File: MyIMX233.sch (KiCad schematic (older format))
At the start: 40 parts, among them IC1 iMX233, IC2 DDR_SDRAM_MT46_x16, J1 USB_A, J2 Micro_SD_Card, SW1 SWITCH_PUSHBUTTON, Y1 24Mhz

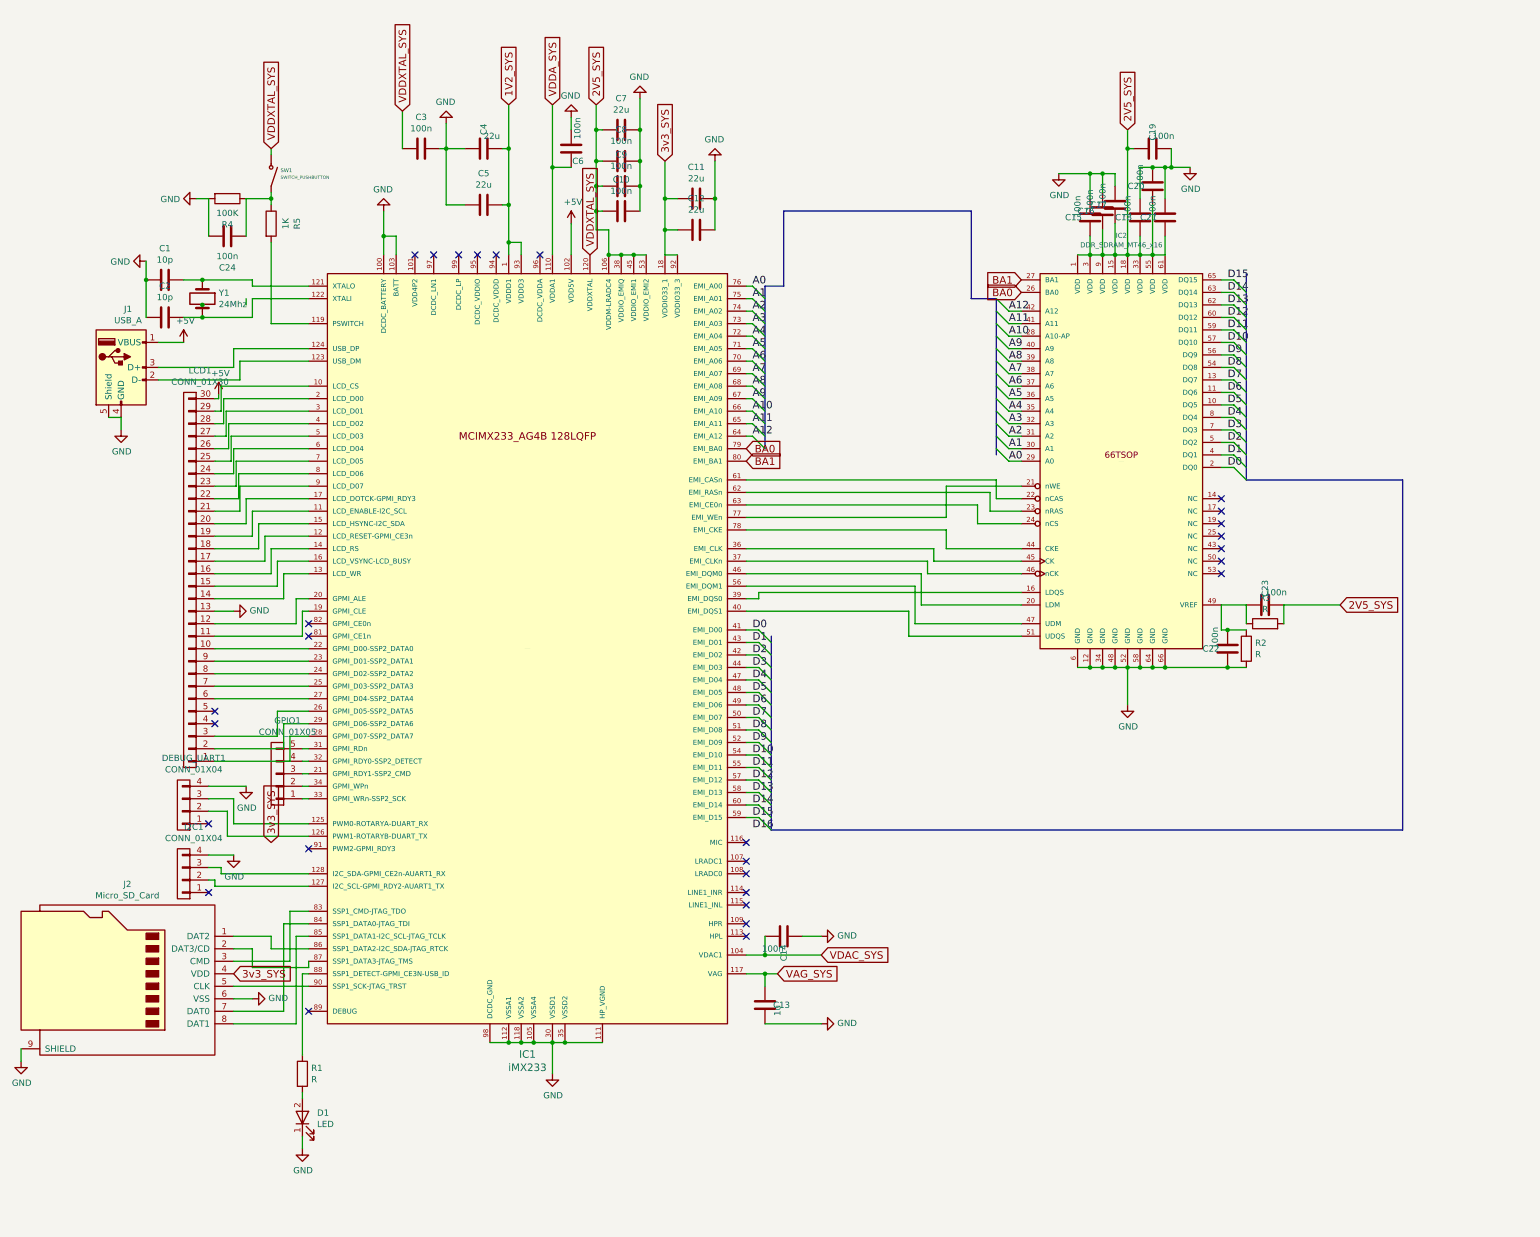
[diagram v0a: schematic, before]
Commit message: footprint mapped
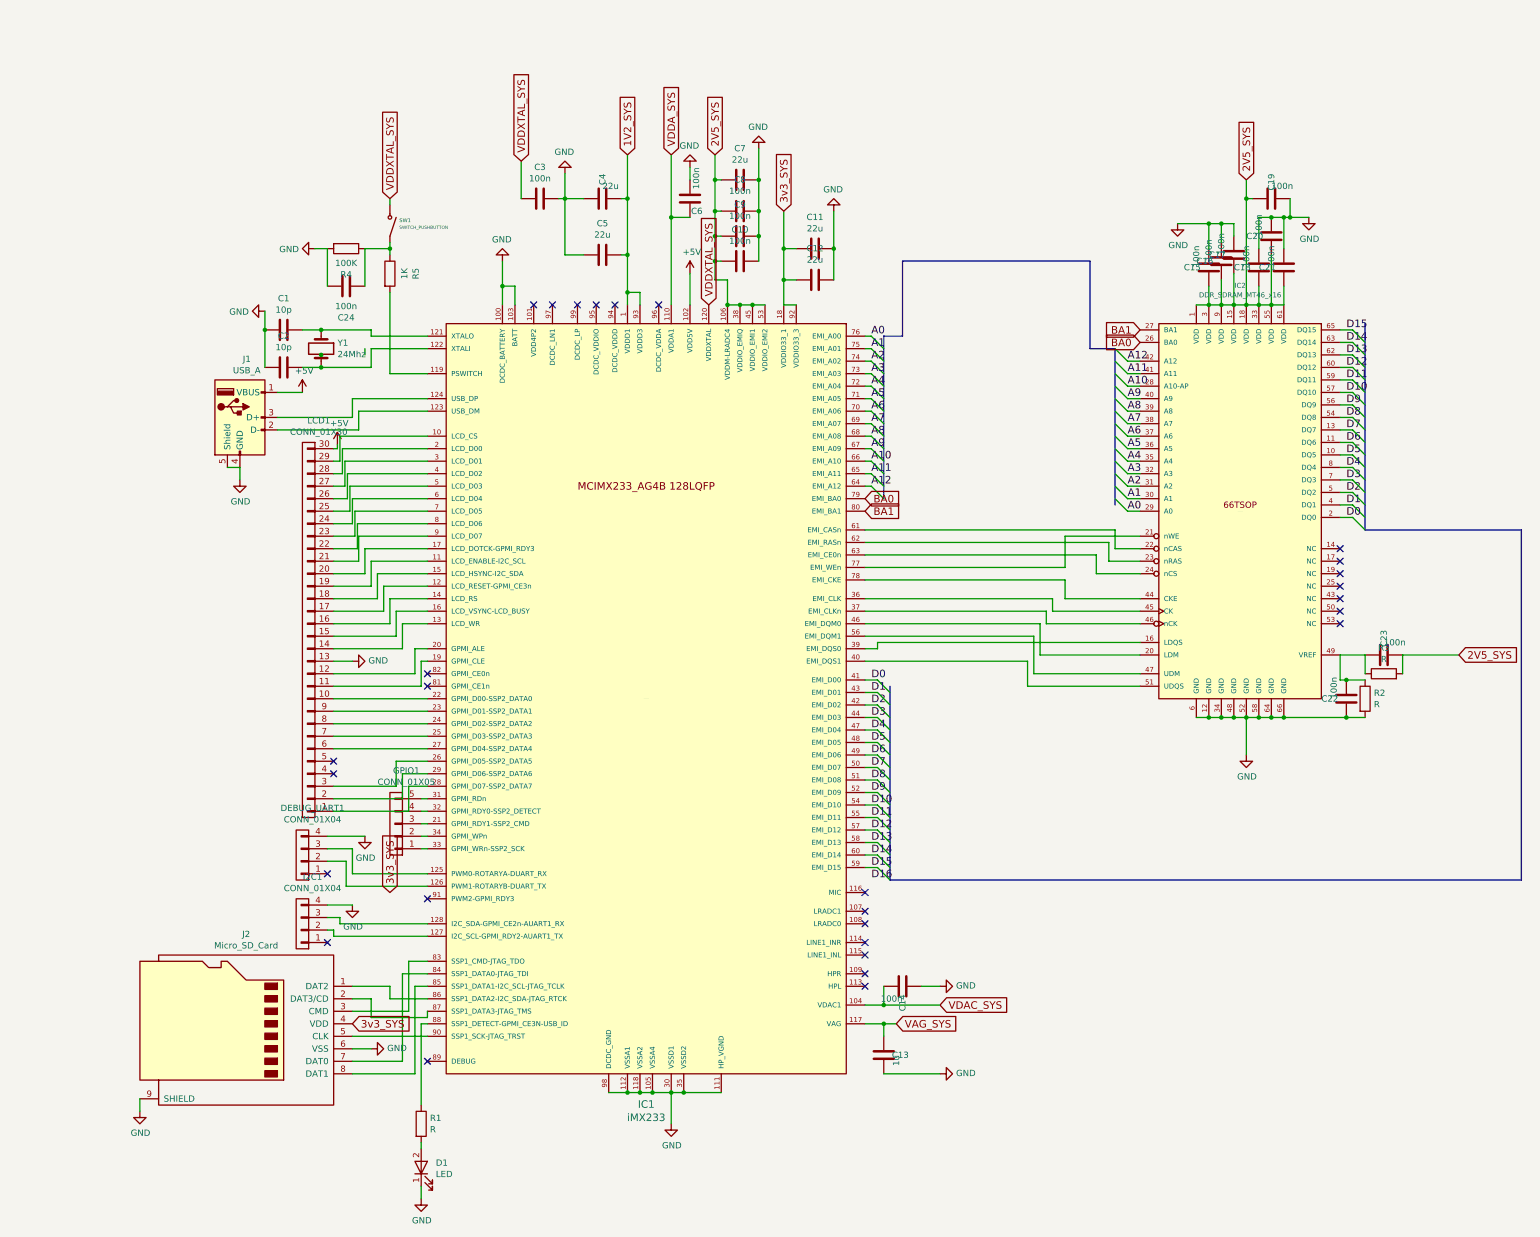
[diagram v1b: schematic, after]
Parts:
- C1, C10, C11, C12, C13, C14, C15, C16, C17, C18, C19, C2, C20, C21, C22, C23, C24, C3, C4, C5, C6, C7, C8, C9: footprint (none) -> Capacitors_SMD:C_0805_HandSoldering
- D1: footprint (none) -> LEDs:LED_D4.0mm
- DEBUG_UART1, I2C1: footprint (none) -> Pin_Headers:Pin_Header_Straight_1x04_Pitch2.54mm
- GPIO1: footprint (none) -> Pin_Headers:Pin_Header_Straight_1x05_Pitch2.54mm
- IC1: footprint (none) -> Housings_QFP:LQFP-128_14x14mm_Pitch0.4mm
- IC2: footprint (none) -> opendous:TSOP66_JEDEC_DDR_SDRAM
- J1: footprint (none) -> Connectors:USB_Micro-B
- J2: footprint (none) -> Connectors_Hirose:microSD_Card_Receptacle_Hirose_DM3AT-SF-PEJM5
- LCD1: footprint (none) -> Pin_Headers:Pin_Header_Straight_1x30_Pitch2.54mm
- R1, R2, R3, R4, R5: footprint (none) -> Resistors_SMD:R_0805_HandSoldering
- SW1: footprint (none) -> Buttons_Switches_THT:SW_PUSH_6mm
- Y1: footprint (none) -> Crystals:Crystal_HC49-4H_Vertical
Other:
- moved on the sheet: C1, C10, C11, C12, C13, C14, C15, C16, C17, C18, C19, C2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

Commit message: pcb without length matching and plot
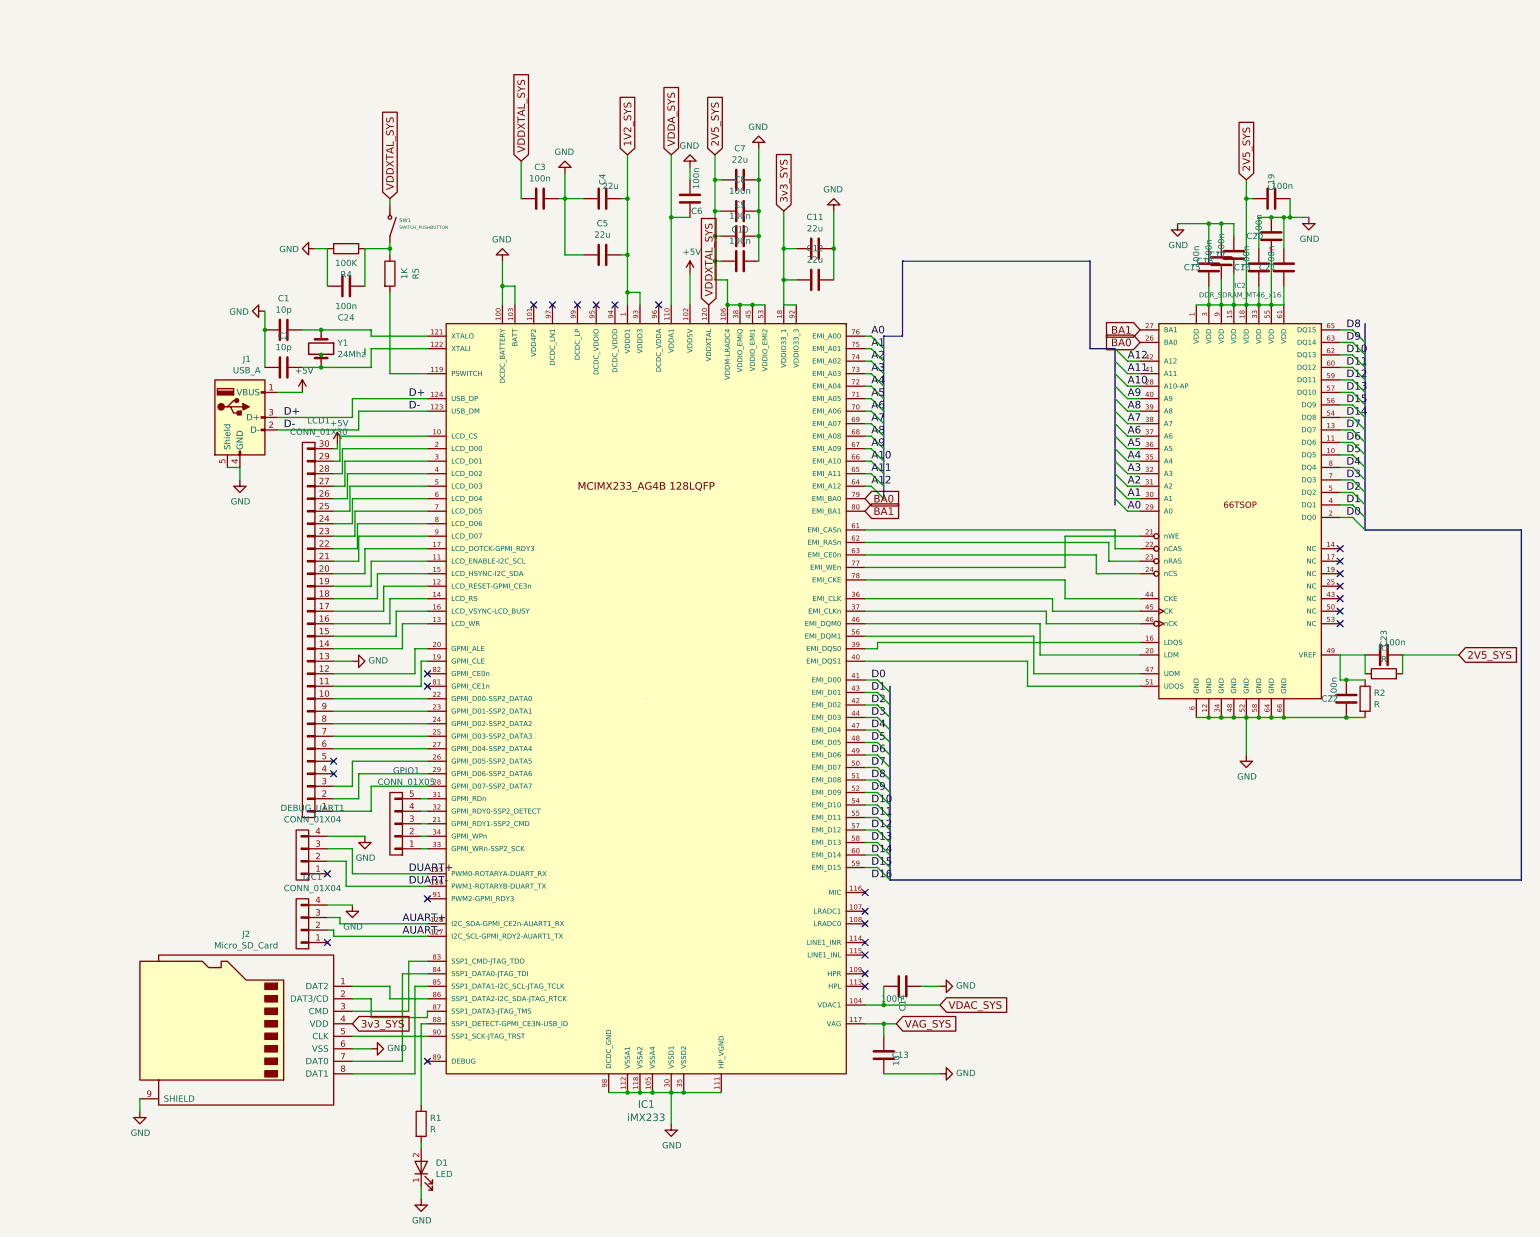
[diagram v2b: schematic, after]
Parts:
- C1, C10, C14, C15, C16, C17, C18, C19, C2, C20, C21, C22, C23, C24, C3, C6, C8, C9: footprint Capacitors_SMD:C_0805_HandSoldering -> Capacitors_SMD:C_0402
- C13: footprint Capacitors_SMD:C_0805_HandSoldering -> Capacitors_SMD:C_0603
- R1, R2, R3, R4, R5: footprint Resistors_SMD:R_0805_HandSoldering -> Resistors_SMD:R_0603
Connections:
- net D10: now also IC2.62 (DQ13); no longer IC2.57 (DQ10)
- net D11: now also IC2.60 (DQ12); no longer IC2.59 (DQ11)
- net D12: now also IC2.59 (DQ11); no longer IC2.60 (DQ12)
- net D13: now also IC2.57 (DQ10); no longer IC2.62 (DQ13)
- net D14: now also IC2.54 (DQ8); no longer IC2.63 (DQ14)
- net D15: now also IC2.56 (DQ9); no longer IC2.65 (DQ15)
- net D8: now also IC2.65 (DQ15); no longer IC2.54 (DQ8)
- net D9: now also IC2.63 (DQ14); no longer IC2.56 (DQ9)
- net D-: now reaches IC1.123 (USB_DM), J1.2 (D-)
- net D+: now reaches IC1.124 (USB_DP), J1.3 (D+)
- net DUART+: now reaches DEBUG_UART1.3 (P3), IC1.125 (PWM0-ROTARYA-DUART_RX)
- net DUART-: now reaches DEBUG_UART1.2 (P2), IC1.126 (PWM1-ROTARYB-DUART_TX)
- net AUART-: now reaches I2C1.2 (P2), IC1.127 (I2C_SCL-GPMI_RDY2-AUART1_TX)
- net AUART+: now reaches I2C1.3 (P3), IC1.128 (I2C_SDA-GPMI_CE2n-AUART1_RX)
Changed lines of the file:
@@
 F 0 "C8" V 5498 2000 50  0000 C CNN
 F 1 "100n" V 5589 2000 50  0000 C CNN
-F 2 "Capacitors_SMD:C_0805_HandSoldering" H 5788 1850 50  0001 C CNN
+F 2 "Capacitors_SMD:C_0402" H 5788 1850 50  0001 C CNN
 F 3 "" H 5750 2000 50  0001 C CNN
 	1    5750 2000
@@
 F 0 "C9" V 5498 2200 50  0000 C CNN
 F 1 "100n" V 5589 2200 50  0000 C CNN
-F 2 "Capacitors_SMD:C_0805_HandSoldering" H 5788 2050 50  0001 C CNN
+F 2 "Capacitors_SMD:C_0402" H 5788 2050 50  0001 C CNN
 F 3 "" H 5750 2200 50  0001 C CNN
 	1    5750 2200
@@
 F 0 "C10" V 5498 2400 50  0000 C CNN
 F 1 "100n" V 5589 2400 50  0000 C CNN
-F 2 "Capacitors_SMD:C_0805_HandSoldering" H 5788 2250 50  0001 C CNN
+F 2 "Capacitors_SMD:C_0402" H 5788 2250 50  0001 C CNN
 F 3 "" H 5750 2400 50  0001 C CNN
 	1    5750 2400
@@
 F 0 "C6" H 5450 1800 50  0000 R CNN
 F 1 "100n" V 5400 2150 50  0000 R CNN
-F 2 "Capacitors_SMD:C_0805_HandSoldering" H 5388 1750 50  0001 C CNN
+F 2 "Capacitors_SMD:C_0402" H 5388 1750 50  0001 C CNN
 F 3 "" H 5350 1900 50  0001 C CNN
 	1    5350 1900
@@
 F 0 "C3" V 4402 1900 50  0000 C CNN
 F 1 "100n" V 4311 1900 50  0000 C CNN
-F 2 "Capacitors_SMD:C_0805_HandSoldering" H 4188 1750 50  0001 C CNN
+F 2 "Capacitors_SMD:C_0402" H 4188 1750 50  0001 C CNN
 F 3 "" H 4150 1900 50  0001 C CNN
 	1    4150 1900
@@
 F 0 "C13" H 7100 8750 50  0000 R CNN
 F 1 "1u" V 7000 8750 50  0000 R CNN
-F 2 "Capacitors_SMD:C_0805_HandSoldering" H 6938 8600 50  0001 C CNN
+F 2 "Capacitors_SMD:C_0603" H 6938 8600 50  0001 C CNN
 F 3 "" H 6900 8750 50  0001 C CNN
 	1    6900 8750
@@
 F 0 "C14" H 7250 8200 50  0000 R CNN
 F 1 "100n" V 7150 8200 50  0000 R CNN
-F 2 "Capacitors_SMD:C_0805_HandSoldering" H 7088 8050 50  0001 C CNN
+F 2 "Capacitors_SMD:C_0402" H 7088 8050 50  0001 C CNN
 F 3 "" H 7050 8200 50  0001 C CNN
 	1    7050 8200
@@
 F 0 "C1" V 2352 2950 50  0000 C CNN
 F 1 "10p" V 2261 2950 50  0000 C CNN
-F 2 "Capacitors_SMD:C_0805_HandSoldering" H 2138 2800 50  0001 C CNN
+F 2 "Capacitors_SMD:C_0402" H 2138 2800 50  0001 C CNN
 F 3 "" H 2100 2950 50  0001 C CNN
 	1    2100 2950
@@
 F 0 "C2" V 2352 3250 50  0000 C CNN
 F 1 "10p" V 2261 3250 50  0000 C CNN
-F 2 "Capacitors_SMD:C_0805_HandSoldering" H 2138 3100 50  0001 C CNN
+F 2 "Capacitors_SMD:C_0402" H 2138 3100 50  0001 C CNN
 F 3 "" H 2100 3250 50  0001 C CNN
 	1    2100 3250
@@
 F 0 "C22" H 10800 5900 50  0000 R CNN
 F 1 "100n" V 10700 5900 50  0000 R CNN
-F 2 "Capacitors_SMD:C_0805_HandSoldering" H 10638 5750 50  0001 C CNN
+F 2 "Capacitors_SMD:C_0402" H 10638 5750 50  0001 C CNN
 F 3 "" H 10600 5900 50  0001 C CNN
 	1    10600 5900
@@
 F 0 "C23" H 11100 5550 50  0000 R CNN
 F 1 "100n" V 11000 5550 50  0000 R CNN
-F 2 "Capacitors_SMD:C_0805_HandSoldering" H 10938 5400 50  0001 C CNN
+F 2 "Capacitors_SMD:C_0402" H 10938 5400 50  0001 C CNN
 F 3 "" H 10900 5550 50  0001 C CNN
 	1    10900 5550
@@
 F 0 "R2" H 10820 5946 50  0000 L CNN
 F 1 "R" H 10820 5855 50  0000 L CNN
-F 2 "Resistors_SMD:R_0805_HandSoldering" V 10680 5900 50  0001 C CNN
+F 2 "Resistors_SMD:R_0603" V 10680 5900 50  0001 C CNN
 F 3 "" H 10750 5900 50  0001 C CNN
 	1    10750 5900
@@
 F 0 "R3" V 11107 5700 50  0000 C CNN
 F 1 "R" V 11016 5700 50  0000 C CNN
-F 2 "Resistors_SMD:R_0805_HandSoldering" V 10830 5700 50  0001 C CNN
+F 2 "Resistors_SMD:R_0603" V 10830 5700 50  0001 C CNN
 F 3 "" H 10900 5700 50  0001 C CNN
 	1    10900 5700
@@
 F 0 "C21" H 10300 2450 50  0000 R CNN
 F 1 "100n" V 10200 2450 50  0000 R CNN
-F 2 "Capacitors_SMD:C_0805_HandSoldering" H 10138 2300 50  0001 C CNN
+F 2 "Capacitors_SMD:C_0402" H 10138 2300 50  0001 C CNN
 F 3 "" H 10100 2450 50  0001 C CNN
 	1    10100 2450
@@
 F 0 "C20" H 10200 2200 50  0000 R CNN
 F 1 "100n" V 10100 2200 50  0000 R CNN
-F 2 "Capacitors_SMD:C_0805_HandSoldering" H 10038 2050 50  0001 C CNN
+F 2 "Capacitors_SMD:C_0402" H 10038 2050 50  0001 C CNN
 F 3 "" H 10000 2200 50  0001 C CNN
 	1    10000 2200
@@
 F 0 "C18" H 10100 2450 50  0000 R CNN
 F 1 "100n" V 10000 2450 50  0000 R CNN
-F 2 "Capacitors_SMD:C_0805_HandSoldering" H 9938 2300 50  0001 C CNN
+F 2 "Capacitors_SMD:C_0402" H 9938 2300 50  0001 C CNN
 F 3 "" H 9900 2450 50  0001 C CNN
 	1    9900 2450
@@
 F 0 "C17" H 9900 2350 50  0000 R CNN
 F 1 "100n" V 9800 2350 50  0000 R CNN
-F 2 "Capacitors_SMD:C_0805_HandSoldering" H 9738 2200 50  0001 C CNN
+F 2 "Capacitors_SMD:C_0402" H 9738 2200 50  0001 C CNN
 F 3 "" H 9700 2350 50  0001 C CNN
 	1    9700 2350
@@
 F 0 "C16" H 9800 2400 50  0000 R CNN
 F 1 "100n" V 9700 2400 50  0000 R CNN
-F 2 "Capacitors_SMD:C_0805_HandSoldering" H 9638 2250 50  0001 C CNN
+F 2 "Capacitors_SMD:C_0402" H 9638 2250 50  0001 C CNN
 F 3 "" H 9600 2400 50  0001 C CNN
 	1    9600 2400
@@
 F 0 "C15" H 9700 2450 50  0000 R CNN
 F 1 "100n" V 9600 2450 50  0000 R CNN
-F 2 "Capacitors_SMD:C_0805_HandSoldering" H 9538 2300 50  0001 C CNN
+F 2 "Capacitors_SMD:C_0402" H 9538 2300 50  0001 C CNN
 F 3 "" H 9500 2450 50  0001 C CNN
 	1    9500 2450
@@
 F 0 "C19" H 10200 1900 50  0000 R CNN
 F 1 "100n" V 10100 1900 50  0000 R CNN
-F 2 "Capacitors_SMD:C_0805_HandSoldering" H 10038 1750 50  0001 C CNN
+F 2 "Capacitors_SMD:C_0402" H 10038 1750 50  0001 C CNN
 F 3 "" H 10000 1900 50  0001 C CNN
 	1    10000 1900
@@
 Text Label 10600 4250 0    60   ~ 0
 D2
+Text Label 10600 3550 0    60   ~ 0
+D15
 Text Label 10600 2950 0    60   ~ 0
-D15
-Text Label 10600 3050 0    60   ~ 0
-D14
-Text Label 10600 3150 0    60   ~ 0
-D13
-Text Label 10600 3250 0    60   ~ 0
-D12
-Text Label 10600 3350 0    60   ~ 0
-D11
-Text Label 10600 3450 0    60   ~ 0
-D10
-Text Label 10600 3550 0    60   ~ 0
-D9
-Text Label 10600 3650 0    60   ~ 0
 D8
 Text Label 10600 3750 0    60   ~ 0
@@
 	1    0    0    -1
 $EndComp
-Text GLabel 2950 7450 1    60   Input ~ 0
-3v3_SYS
 $Comp
 L CONN_01X04 DEBUG_UART1
@@
 	2800 8700 2650 8700
 Wire Wire Line
-	2500 6800 3100 6800
-Wire Wire Line
-	3100 6800 3100 6600
-Wire Wire Line
-	3100 6600 3250 6600
-Wire Wire Line
-	2500 6700 3050 6700
-Wire Wire Line
-	3050 6700 3050 6500
-Wire Wire Line
-	3050 6500 3250 6500
-Wire Wire Line
-	3250 6400 3000 6400
-Wire Wire Line
-	3000 6400 3000 6600
-Wire Wire Line
-	3000 6600 2500 6600
+	2800 6600 3250 6600
+Wire Wire Line
+	2700 6500 3250 6500
 Wire Wire Line
 	2500 6300 3250 6300
@@
 F 0 "R1" H 3270 9346 50  0000 L CNN
 F 1 "R" H 3270 9255 50  0000 L CNN
-F 2 "Resistors_SMD:R_0805_HandSoldering" V 3130 9300 50  0001 C CNN
+F 2 "Resistors_SMD:R_0603" V 3130 9300 50  0001 C CNN
 F 3 "" H 3200 9300 50  0001 C CNN
 	1    3200 9300
@@
 F 0 "C24" V 2348 2600 50  0000 C CNN
 F 1 "100n" V 2439 2600 50  0000 C CNN
-F 2 "Capacitors_SMD:C_0805_HandSoldering" H 2638 2450 50  0001 C CNN
+F 2 "Capacitors_SMD:C_0402" H 2638 2450 50  0001 C CNN
 F 3 "" H 2600 2600 50  0001 C CNN
 	1    2600 2600
@@
 F 0 "R5" V 3157 2500 50  0000 C CNN
 F 1 "1K" V 3066 2500 50  0000 C CNN
-F 2 "Resistors_SMD:R_0805_HandSoldering" V 2880 2500 50  0001 C CNN
+F 2 "Resistors_SMD:R_0603" V 2880 2500 50  0001 C CNN
 F 3 "" H 2950 2500 50  0001 C CNN
 	1    2950 2500
@@
 F 0 "R4" V 2807 2300 50  0000 C CNN
 F 1 "100K" V 2716 2300 50  0000 C CNN
-F 2 "Resistors_SMD:R_0805_HandSoldering" V 2530 2300 50  0001 C CNN
+F 2 "Resistors_SMD:R_0603" V 2530 2300 50  0001 C CNN
 F 3 "" H 2600 2300 50  0001 C CNN
 	1    2600 2300
@@
 Wire Wire Line
 	2450 2300 2350 2300
+Text Label 10600 3050 0    60   ~ 0
+D9
+Text Label 10600 3150 0    60   ~ 0
+D10
+Text Label 10600 3250 0    60   ~ 0
+D11
+Text Label 10600 3350 0    60   ~ 0
+D12
+Text Label 10600 3450 0    60   ~ 0
+D13
+Text Label 10600 3650 0    60   ~ 0
+D14
+Text Label 3100 3500 0    60   ~ 0
+D+
+Text Label 3100 3600 0    60   ~ 0
+D-
+Text Label 2100 3650 0    60   ~ 0
+D+
+Text Label 2100 3750 0    60   ~ 0
+D-
+Text Label 3050 7700 0    60   ~ 0
+AUART+
+Text Label 3050 7800 0    60   ~ 0
+AUART-
+Text Label 3100 7300 0    60   ~ 0
+DUART+
+Text Label 3100 7400 0    60   ~ 0
+DUART-
+Wire Wire Line
+	3250 6400 2650 6400
+Wire Wire Line
+	2650 6400 2650 6600
+Wire Wire Line
+	2650 6600 2500 6600
+Wire Wire Line
+	2700 6500 2700 6700
+Wire Wire Line
+	2700 6700 2500 6700
+Wire Wire Line
+	2800 6600 2800 6800
+Wire Wire Line
+	2800 6800 2500 6800
 $EndSCHEMATC
